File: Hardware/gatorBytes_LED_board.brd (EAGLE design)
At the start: 110.5 x 57.1 mm, 132 parts

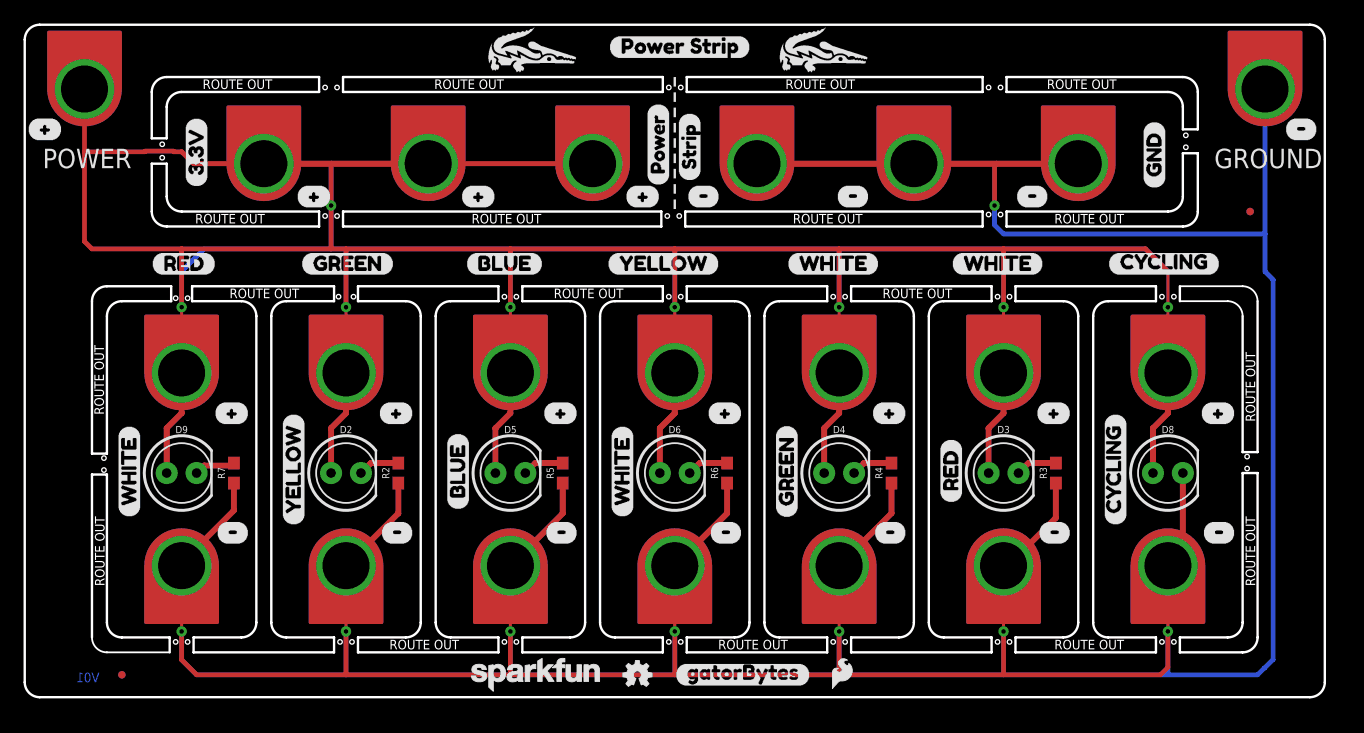
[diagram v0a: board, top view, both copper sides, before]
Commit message: removing pth
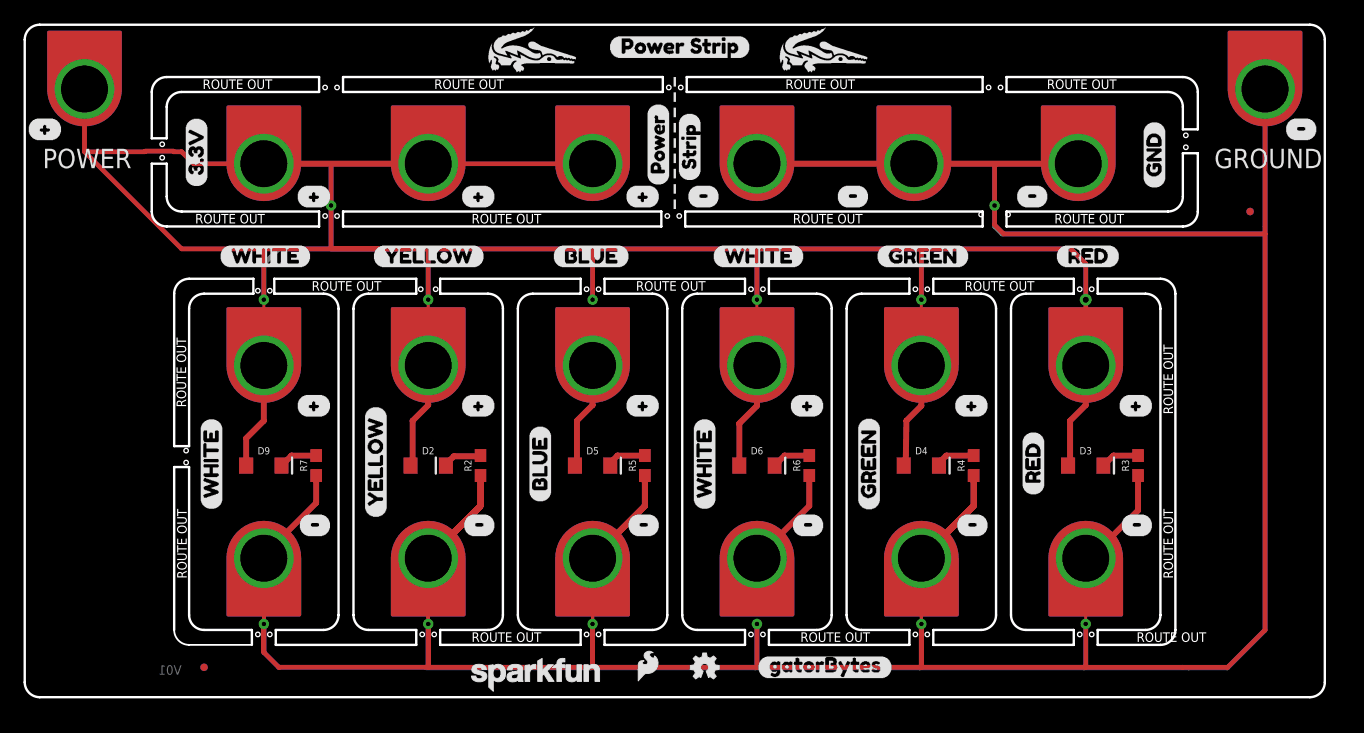
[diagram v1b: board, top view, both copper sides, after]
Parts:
- removed D8: (no value), SparkFun-LED:LED_5MM-KIT
- removed LOGO14: SFE_LOGO_FLAME.1_INCH, SparkFun-Aesthetics:SFE_LOGO_FLAME_.1
- removed LOGO8: OSHW-LOGOMINI, SparkFun-Aesthetics:OSHW-LOGO-MINI
- removed U$4, U$9: GATOR_MINI, TAB:GATOR_MINI
- removed U$43, U$59, U$80: (no value), gatorbytes:CYCLING11
- removed U$51, U$88: (no value), gatorbytes:#8
- removed U$52, U$94: (no value), gatorbytes:#9
- removed U$74: (no value), gator#PNG (6):GATOR#PNG
- D2: device SparkFun-LED:LED_5MM -> SparkFun-LED:LED-1206-HIDDENSILK
- D3: value (none) -> RED; device SparkFun-LED:LED_5MM -> SparkFun-LED:LED-1206
- D4: value (none) -> GREEN; device SparkFun-LED:LED_5MM -> SparkFun-LED:LED-1206
- D5: value (none) -> BLUE; device SparkFun-LED:LED_5MM -> SparkFun-LED:LED-1206
- D6, D9: value (none) -> WHITE; device SparkFun-LED:LED_5MM -> SparkFun-LED:LED-1206
- moved U$41 76.8 mm to (87.6, 37.5)
- moved U$13 48.9 mm to (48.3, 33.0)
- moved U$39 48.9 mm to (72.4, 37.5)
- moved U$45 48.3 mm to (16.5, 37.5)
- moved U$7 34.9 mm to (62.2, 6.99)
- moved U$44 20.3 mm to (58.4, 37.5)
- moved U$48 19.9 mm to (29.6, 37.5)
- moved LOGO17 16.5 mm to (51.8, 1.02)
- moved U$36 7.39 mm to (44.8, 37.5)
- moved LOGO9 7.01 mm to (35.6, 15.2)
- moved U$68 7.01 mm to (16.1, 20.1)
- moved U$82 7.01 mm to (14.6, 14.0)
- moved D2 7.01 mm to (34.3, 19.7)
- moved D3 7.01 mm to (90.2, 19.7)
- moved D4 7.01 mm to (76.2, 19.7)
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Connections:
- net 3.3V: no longer D8.A, U$4.P1
- net GND: no longer D8.K, U$9.P1
- net N$1: now also D2.C; no longer D2.K
- net N$3: now also D3.C; no longer D3.K
- net N$4: now also D4.C; no longer D4.K
- net N$5: now also D5.C; no longer D5.K
- net N$6: now also D6.C; no longer D6.K
- net N$7: now also D9.C; no longer D9.K
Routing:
- net GND: track 458.1 -> 682.2 mm, vias 8 -> 7
- net 3.3V: track 429.6 -> 382.6 mm, vias 8 -> 7
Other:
- outline, holes or cut-outs redrawn

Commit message: pre design review
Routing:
- net GND: track 682.2 -> 632.8 mm
- net 3.3V: track 382.6 -> 374.1 mm, vias 7 -> 8

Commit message: post checklist changes
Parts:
- removed U$66: (no value), gatorbytes:GATORBYTES9
- added U$4: (no value), SparkFun-Aesthetics:ORDERING_INSTRUCTIONS
- added U$43: (no value), buzzard_labels (6):POWER2
- added U$51: (no value), buzzard_labels (9):GATOR#COLOR0
- added U$9: (no value), buzzard_labels (6):GROUND3
- D2: value (none) -> RED; device SparkFun-LED:LED-1206-HIDDENSILK -> SparkFun-LED:LED-1206
- D3: value RED -> WHITE
- D5: value BLUE -> Yellow
- D6: value WHITE -> GREEN
- U$1, U$10, U$11, U$13, U$16, U$18, U$19, U$2, U$20, U$21, U$28, U$3, U$30, U$32, U$33, U$34, U$38, U$6, U$7, U$8: value GATOR_MINI -> TAB_GATOR_MINI; device TAB:GATOR_MINI -> SparkFun-Connectors:TAB_GATOR_MINI
- moved U$17 55.9 mm to (38.7, 22.2)
- moved U$42 55.9 mm to (29.8, 17.1)
- moved U$37 27.9 mm to (71.8, 16.5)
- moved U$46 27.9 mm to (85.7, 15.9)
- moved U$75 27.9 mm to (80.6, 22.9)
- moved U$78 27.9 mm to (94.6, 23.5)
- moved U$40 14.0 mm to (57.8, 15.9)
- moved U$49 14.0 mm to (43.8, 15.2)
- moved U$67 14.0 mm to (66.7, 23.5)
- moved U$76 14.0 mm to (52.7, 24.0)
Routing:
- net GND: track 632.8 -> 723.0 mm, vias 7 -> 2
- net 3.3V: track 374.1 -> 415.0 mm, vias 8 -> 2
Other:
- board text added: "Black PCB"
- board text added: "v10"
- board text removed: "GROUND"
- board text removed: "POWER"
- board text removed: "V01"

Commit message: post checklist changes
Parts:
- added LOGO8: REVISION, SparkFun-Aesthetics:REVISION
- D4: value GREEN -> BLUE
- R5: value 150 -> 330
- R6: value 330 -> 150
- moved U$41 56.0 mm to (31.6, 37.5)
- moved U$36 28.6 mm to (73.4, 37.5)
- moved U$44 27.9 mm to (86.4, 37.5)
- moved U$39 14.0 mm to (58.4, 37.5)
- moved U$48 14.0 mm to (43.6, 37.5)
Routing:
- net GND: track 723.0 -> 723.8 mm, vias 2 -> 1
- net 3.3V: vias 2 -> 1
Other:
- board text added: "A. England"
- board text added: "Black Gloss PCB"
- board text removed: "Black PCB"
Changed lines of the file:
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@@
 <wire x1="81.407" y1="40.005" x2="81.407" y2="41.275" width="0.2032" layer="20"/>
 <wire x1="81.407" y1="41.275" x2="56.134" y2="41.275" width="0.2032" layer="20"/>
-<text x="49.53" y="-8.89" size="1.778" layer="51">M. West</text>
+<text x="49.53" y="-8.89" size="1.778" layer="51" font="vector">M. West</text>
 <dimension x1="1.27" y1="1.27" x2="0.56553125" y2="0.213296875" x3="-3.761128125" y3="-6.276696875" textsize="1.778" layer="47" dtype="radius" unit="inch"/>
 <dimension x1="109.22" y1="1.27" x2="110.118025" y2="0.371975" x3="111.82345625" y3="-8.95345625" textsize="1.778" layer="47" dtype="radius" unit="inch"/>
@@
 <wire x1="97.79" y1="5.715" x2="97.79" y2="34.29" width="0.2032" layer="20"/>
 <wire x1="91.186" y1="35.56" x2="96.52" y2="35.56" width="0.2032" layer="20"/>
-<text x="4.445" y="-24.13" size="1.778" layer="51">Black PCB</text>
-<text x="109.22" y="0" size="1.27" layer="16" font="vector" ratio="20" rot="MR0">v10</text>
+<text x="4.445" y="-24.13" size="1.778" layer="51">Black Gloss PCB</text>
+<text x="109.22" y="0" size="1.778" layer="16" font="vector" ratio="20" rot="MR0">v10</text>
+<text x="48.26" y="-11.43" size="1.778" layer="51" font="vector">A. England</text>
 </plain>
 <attributes>
@@
 <attribute name="VALUE" value="WHITE" x="90.17" y="19.685" size="1.778" layer="27" display="off"/>
 </element>
-<element name="D4" library="SparkFun-LED" package="LED-1206" value="GREEN" x="76.2" y="19.685">
-<attribute name="PROD_ID" value="DIO-00862" x="76.2" y="19.685" size="1.778" layer="27" display="off"/>
-<attribute name="VALUE" value="GREEN" x="76.2" y="19.685" size="1.778" layer="27" display="off"/>
+<element name="D4" library="SparkFun-LED" package="LED-1206" value="BLUE" x="76.2" y="19.685">
+<attribute name="PROD_ID" value="DIO-09911" x="76.2" y="19.685" size="1.778" layer="27" display="off"/>
+<attribute name="VALUE" value="BLUE" x="76.2" y="19.685" size="1.778" layer="27" display="off"/>
 </element>
 <element name="D5" library="SparkFun-LED" package="LED-1206" value="Yellow" x="48.26" y="19.685">
@@
 <attribute name="PROD_ID" value="RES-11028" x="80.645" y="19.685" size="1.778" layer="27" rot="R90" display="off"/>
 </element>
-<element name="R5" library="SparkFun-Resistors" package="0603" value="150" x="52.705" y="19.685" rot="R90">
-<attribute name="PROD_ID" value="RES-11028" x="52.705" y="19.685" size="1.778" layer="27" rot="R90" display="off"/>
-</element>
-<element name="R6" library="SparkFun-Resistors" package="0603" value="330" x="66.675" y="19.685" rot="R90">
-<attribute name="PROD_ID" value="RES-00818" x="66.675" y="19.685" size="1.778" layer="27" rot="R90" display="off"/>
+<element name="R5" library="SparkFun-Resistors" package="0603" value="330" x="52.705" y="19.685" rot="R90">
+<attribute name="PROD_ID" value="RES-00818" x="52.705" y="19.685" size="1.778" layer="27" rot="R90" display="off"/>
+</element>
+<element name="R6" library="SparkFun-Resistors" package="0603" value="150" x="66.675" y="19.685" rot="R90">
+<attribute name="PROD_ID" value="RES-11028" x="66.675" y="19.685" size="1.778" layer="27" rot="R90" display="off"/>
 </element>
 <element name="R7" library="SparkFun-Resistors" package="0603" value="330" x="24.765" y="19.685" rot="R90">
@@
 <element name="U$33" library="SparkFun-Connectors" package="TAB_GATOR_MINI" value="TAB_GATOR_MINI" x="20.32" y="33.02" rot="R180"/>
 <element name="U$34" library="SparkFun-Connectors" package="TAB_GATOR_MINI" value="TAB_GATOR_MINI" x="34.29" y="50.165" rot="R180"/>
-<element name="U$36" library="gatorbytes" package="BLUE4" value="" x="44.831" y="37.465"/>
+<element name="U$36" library="gatorbytes" package="BLUE4" value="" x="73.406" y="37.465"/>
 <element name="U$37" library="gatorbytes" package="BLUE4" value="" x="71.755" y="16.51" rot="R90"/>
-<element name="U$39" library="gatorbytes" package="GREEN3" value="" x="72.39" y="37.465"/>
+<element name="U$39" library="gatorbytes" package="GREEN3" value="" x="58.42" y="37.465"/>
 <element name="U$40" library="gatorbytes" package="GREEN3" value="" x="57.785" y="15.875" rot="R90"/>
-<element name="U$41" library="gatorbytes" package="RED2" value="" x="87.63" y="37.465"/>
+<element name="U$41" library="gatorbytes" package="RED2" value="" x="31.623" y="37.465"/>
 <element name="U$42" library="gatorbytes" package="RED2" value="" x="29.845" y="17.145" rot="R90"/>
-<element name="U$44" library="gatorbytes" package="WHITE6" value="" x="58.42" y="37.465"/>
+<element name="U$44" library="gatorbytes" package="WHITE6" value="" x="86.36" y="37.465"/>
 <element name="U$45" library="gatorbytes" package="WHITE6" value="" x="16.51" y="37.465"/>
 <element name="U$46" library="gatorbytes" package="WHITE6" value="" x="85.725" y="15.875" rot="R90"/>
 <element name="U$47" library="gatorbytes" package="WHITE6" value="" x="15.875" y="15.875" rot="R90"/>
-<element name="U$48" library="gatorbytes" package="YELLOW5" value="" x="29.591" y="37.465"/>
+<element name="U$48" library="gatorbytes" package="YELLOW5" value="" x="43.561" y="37.465"/>
 <element name="U$49" library="gatorbytes" package="YELLOW5" value="" x="43.815" y="15.24" rot="R90"/>
 <element name="U$53" library="gatorbytes" package="#8" value="" x="95.885" y="24.765" rot="R180"/>
@@
 <element name="U$51" library="buzzard_labels (9)" package="GATOR#COLOR0" value="" x="60.579" y="2.286"/>
 <element name="U$4" library="SparkFun-Aesthetics" package="ORDERING_INSTRUCTIONS" value="" x="3.175" y="-12.065"/>
+<element name="LOGO8" library="SparkFun-Aesthetics" package="REVISION" value="REVISION" x="33.655" y="-11.43"/>
 </elements>
 <signals>
@@
 <wire x1="76.2" y1="27.305" x2="76.2" y2="24.13" width="0.508" layer="1"/>
 <wire x1="88.8425" y1="19.685" x2="88.8425" y2="23.495" width="0.508" layer="1"/>
-<via x="26.035" y="41.783" extent="1-16" drill="0.381"/>
 <wire x1="32.258003125" y1="38.1" x2="26.035003125" y2="38.1" width="0.4064" layer="16"/>
 <wire x1="26.035" y1="38.1" x2="21.59" y2="38.1" width="0.4064" layer="16"/>
@@
 <wire x1="20.32" y1="45.339" x2="26.035" y2="45.339" width="0.4064" layer="16"/>
 <wire x1="26.035" y1="45.339" x2="34.29" y2="45.339" width="0.4064" layer="16"/>
-<wire x1="26.035" y1="41.783" x2="26.035" y2="45.339" width="0.4064" layer="16"/>
 <wire x1="34.29" y1="45.339" x2="48.26" y2="45.339" width="0.4064" layer="1"/>
 <contactref element="U$32" pad="P1"/>
@@
 <wire x1="74.7" y1="22.63" x2="74.7" y2="19.685" width="0.508" layer="1"/>
 <wire x1="48.26" y1="24.1875" x2="48.26" y2="24.8225" width="0.508" layer="1"/>
-<wire x1="26.035" y1="41.783" x2="26.035003125" y2="41.782996875" width="0.4064" layer="16"/>
+<wire x1="26.035003125" y1="41.782996875" x2="26.035" y2="41.783" width="0.4064" layer="16"/>
 <wire x1="26.035003125" y1="41.782996875" x2="26.035003125" y2="38.1" width="0.4064" layer="16"/>
 <wire x1="20.32" y1="36.83" x2="20.32" y2="28.194" width="0.4064" layer="16"/>
@@
 <wire x1="34.29" y1="38.1" x2="34.29" y2="28.194" width="0.4064" layer="16"/>
 <wire x1="34.29" y1="28.194" x2="34.29" y2="38.1" width="0.4064" layer="1"/>
+<wire x1="26.035" y1="41.783" x2="26.035" y2="45.339" width="0.4064" layer="16"/>
 </signal>
 <signal name="GND">
@@
 <wire x1="80.645" y1="16.256" x2="76.2" y2="11.811" width="0.508" layer="1"/>
 <via x="90.17" y="6.223" extent="1-16" drill="0.381"/>
-<via x="62.23" y="6.223" extent="1-16" drill="0.381"/>
 <wire x1="102.20660625" y1="2.4892" x2="34.1376" y2="2.4892" width="0.4064" layer="16"/>
 <wire x1="34.29" y1="2.54" x2="21.59" y2="2.54" width="0.4064" layer="16"/>
 <wire x1="21.59" y1="2.54" x2="20.32" y2="3.81" width="0.4064" layer="16"/>
 <wire x1="90.17" y1="6.223" x2="90.17" y2="2.54" width="0.4064" layer="16"/>
-<wire x1="62.23" y1="6.223" x2="62.23" y2="2.54" width="0.4064" layer="16"/>
 <wire x1="82.423" y1="41.783" x2="82.423" y2="45.339" width="0.4064" layer="16"/>
 <wire x1="82.423" y1="45.339" x2="75.565" y2="45.339" width="0.4064" layer="16"/>
@@
 <wire x1="34.29" y1="2.54" x2="34.29" y2="11.811" width="0.4064" layer="16"/>
 <wire x1="34.29" y1="11.811" x2="34.29" y2="6.223" width="0.4064" layer="1"/>
+<wire x1="62.23" y1="2.54" x2="62.23" y2="6.985" width="0.4064" layer="16"/>
 </signal>
 <signal name="N$1">
